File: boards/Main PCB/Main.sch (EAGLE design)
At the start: 89 parts, among them CN1 MINIB, CN2 MINIB, IC1 FT232RL, IC2 FT232RL, J1 3_PIN_JST-XH, J2 2_PIN_JST-XH, Q4 BSS138, Q5 BSS138, Q6 BSS138, Q7 BSS138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

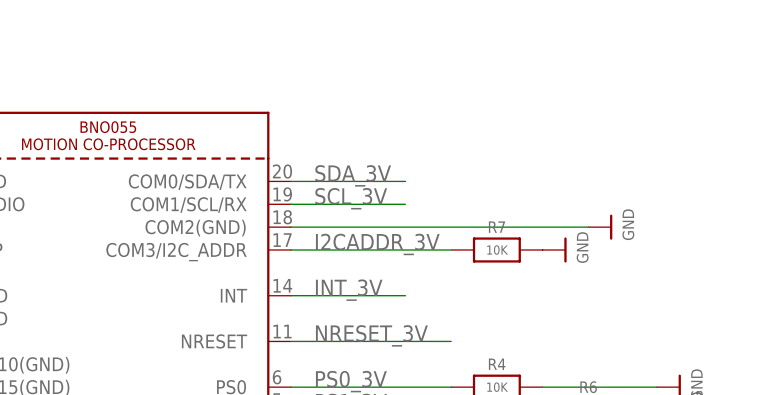
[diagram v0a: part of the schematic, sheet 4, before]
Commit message: Added pullup resistors for SDA and SCL
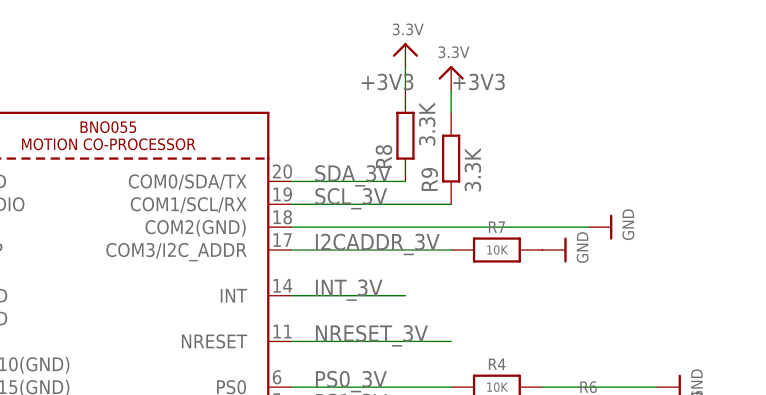
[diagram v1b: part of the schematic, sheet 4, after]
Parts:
- added R8, R9: 3.3K, resistor:R-EU_R0805
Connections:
- net +3V3: now also R8.2, R9.2
- net SCL_3V: now also R9.1
- net SDA_3V: now also R8.1
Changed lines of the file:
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@@
 <?xml version="1.0" encoding="utf-8"?>
 <!DOCTYPE eagle SYSTEM "eagle.dtd">
-<eagle version="9.2.2">
+<eagle version="9.3.1">
 <drawing>
 <settings>
@@
 <part name="JP4" library="microbuilder" deviceset="HEADER-1X4" device="76MIL"/>
 <part name="JP5" library="main_library" deviceset="MICROBUILDER_HEADER-1X6" device="76MIL"/>
+<part name="R8" library="resistor" library_urn="urn:adsk.eagle:library:348" deviceset="R-EU_" device="R0805" package3d_urn="urn:adsk.eagle:package:26059/1" value="3.3K"/>
+<part name="R9" library="resistor" library_urn="urn:adsk.eagle:library:348" deviceset="R-EU_" device="R0805" package3d_urn="urn:adsk.eagle:package:26059/1" value="3.3K"/>
+<part name="U$2" library="microbuilder" deviceset="3.3V" device=""/>
+<part name="U$4" library="microbuilder" deviceset="3.3V" device=""/>
 </parts>
 <sheets>
@@
 <attribute name="VALUE" x="-29.21" y="-71.12" size="1.778" layer="96"/>
 </instance>
+<instance part="R8" gate="G$1" x="-17.78" y="10.16" smashed="yes" rot="R90">
+<attribute name="NAME" x="-19.2786" y="6.35" size="1.778" layer="95" rot="R90"/>
+<attribute name="VALUE" x="-14.478" y="8.89" size="1.778" layer="96" rot="R90"/>
+</instance>
+<instance part="R9" gate="G$1" x="-12.7" y="7.62" smashed="yes" rot="R90">
+<attribute name="NAME" x="-14.1986" y="3.81" size="1.778" layer="95" rot="R90"/>
+<attribute name="VALUE" x="-9.398" y="3.81" size="1.778" layer="96" rot="R90"/>
+</instance>
+<instance part="U$2" gate="G$1" x="-17.78" y="20.32" smashed="yes">
+<attribute name="VALUE" x="-19.304" y="21.336" size="1.27" layer="96"/>
+</instance>
+<instance part="U$4" gate="G$1" x="-12.7" y="17.78" smashed="yes">
+<attribute name="VALUE" x="-14.224" y="18.796" size="1.27" layer="96"/>
+</instance>
 </instances>
 <busses>
@@
 <wire x1="-30.48" y1="5.08" x2="-17.78" y2="5.08" width="0.1524" layer="91"/>
 <label x="-27.94" y="5.08" size="1.778" layer="95"/>
+<pinref part="R8" gate="G$1" pin="1"/>
 </segment>
 <segment>
@@
 <segment>
 <pinref part="U$3" gate="G$1" pin="COM1/SCL/RX"/>
-<wire x1="-30.48" y1="2.54" x2="-17.78" y2="2.54" width="0.1524" layer="91"/>
+<wire x1="-30.48" y1="2.54" x2="-12.7" y2="2.54" width="0.1524" layer="91"/>
 <label x="-27.94" y="2.54" size="1.778" layer="95"/>
+<pinref part="R9" gate="G$1" pin="1"/>
 </segment>
 <segment>
@@
 <label x="-45.72" y="-55.88" size="1.778" layer="95"/>
 </segment>
-</net>
+<segment>
+<pinref part="R8" gate="G$1" pin="2"/>
+<pinref part="U$2" gate="G$1" pin="3.3V"/>
+<wire x1="-17.78" y1="17.78" x2="-17.78" y2="15.24" width="0.1524" layer="91"/>
+<label x="-22.86" y="15.24" size="1.778" layer="95"/>
+</segment>
+<segment>
+<pinref part="R9" gate="G$1" pin="2"/>
+<pinref part="U$4" gate="G$1" pin="3.3V"/>
+<wire x1="-12.7" y1="15.24" x2="-12.7" y2="12.7" width="0.1524" layer="91"/>
+<label x="-12.7" y="15.24" size="1.778" layer="95"/>
+</segment>
+</net>

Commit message: Added indicator LEDs to board and cleaned up iOS assets
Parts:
- added R10, R11, R32: 1K, rcl:R-US_R0805
- added RX2, RX3, RX4: Green, adafruit:LEDCHIP-LED0805
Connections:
- removed net TEST_GPIO4: U2.PB4/SPI1_MISO/TIM17_BKIN/TIM3_CH1/EVENTOUT
- new net N$12: R32.2, RX4.C
- new net N$13: RX2.C, U2.PB4/SPI1_MISO/TIM17_BKIN/TIM3_CH1/EVENTOUT
- new net N$3: R10.1, RX2.A
- new net N$4: R11.2, RX3.C
- net +3V3: now also R10.2, RX3.A
- net +5V: now also RX4.A
- net GND: now also R11.1, R32.1
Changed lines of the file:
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@@
 <?xml version="1.0" encoding="utf-8"?>
 <!DOCTYPE eagle SYSTEM "eagle.dtd">
-<eagle version="9.3.1">
+<eagle version="9.3.0">
 <drawing>
 <settings>
@@
 <part name="U$2" library="microbuilder" deviceset="3.3V" device=""/>
 <part name="U$4" library="microbuilder" deviceset="3.3V" device=""/>
+<part name="R10" library="rcl" library_urn="urn:adsk.eagle:library:334" deviceset="R-US_" device="R0805" package3d_urn="urn:adsk.eagle:package:23553/2" value="1K"/>
+<part name="RX2" library="adafruit" deviceset="LED" device="CHIP-LED0805" value="Green"/>
+<part name="+3V10" library="supply1" library_urn="urn:adsk.eagle:library:371" deviceset="+3V3" device=""/>
+<part name="RX3" library="adafruit" deviceset="LED" device="CHIP-LED0805" value="Green"/>
+<part name="R11" library="rcl" library_urn="urn:adsk.eagle:library:334" deviceset="R-US_" device="R0805" package3d_urn="urn:adsk.eagle:package:23553/2" value="1K"/>
+<part name="+3V11" library="supply1" library_urn="urn:adsk.eagle:library:371" deviceset="+3V3" device=""/>
+<part name="RX4" library="adafruit" deviceset="LED" device="CHIP-LED0805" value="Green"/>
+<part name="R32" library="rcl" library_urn="urn:adsk.eagle:library:334" deviceset="R-US_" device="R0805" package3d_urn="urn:adsk.eagle:package:23553/2" value="1K"/>
+<part name="GND33" library="supply1" library_urn="urn:adsk.eagle:library:371" deviceset="GND" device=""/>
 </parts>
 <sheets>
@@
 <attribute name="NAME" x="149.225" y="176.53" size="1.778" layer="95" rot="R90"/>
 <attribute name="VALUE" x="157.48" y="176.53" size="1.778" layer="96" rot="R90"/>
+</instance>
+<instance part="R10" gate="G$1" x="370.84" y="137.16" smashed="yes">
+<attribute name="VALUE" x="367.03" y="138.938" size="1.778" layer="96"/>
+</instance>
+<instance part="RX2" gate="G$1" x="360.68" y="137.16" smashed="yes" rot="R270">
+<attribute name="NAME" x="358.648" y="138.684" size="1.778" layer="95"/>
+<attribute name="VALUE" x="354.33" y="135.255" size="1.778" layer="96"/>
+</instance>
+<instance part="+3V10" gate="G$1" x="381" y="142.24" smashed="yes">
+<attribute name="VALUE" x="378.46" y="137.16" size="1.778" layer="96" rot="R90"/>
+</instance>
+<instance part="RX3" gate="G$1" x="370.84" y="198.12" smashed="yes">
+<attribute name="NAME" x="369.316" y="196.088" size="1.778" layer="95" rot="R90"/>
+<attribute name="VALUE" x="372.745" y="191.77" size="1.778" layer="96" rot="R90"/>
+</instance>
+<instance part="R11" gate="G$1" x="370.84" y="185.42" smashed="yes" rot="R90">
+<attribute name="VALUE" x="369.062" y="181.61" size="1.778" layer="96" rot="R90"/>
+</instance>
+<instance part="+3V11" gate="G$1" x="370.84" y="208.28" smashed="yes">
+<attribute name="VALUE" x="368.3" y="203.2" size="1.778" layer="96" rot="R90"/>
+</instance>
+<instance part="RX4" gate="G$1" x="22.86" y="254" smashed="yes">
+<attribute name="NAME" x="21.336" y="251.968" size="1.778" layer="95" rot="R90"/>
+<attribute name="VALUE" x="24.765" y="247.65" size="1.778" layer="96" rot="R90"/>
+</instance>
+<instance part="R32" gate="G$1" x="22.86" y="241.3" smashed="yes" rot="R90">
+<attribute name="VALUE" x="21.082" y="237.49" size="1.778" layer="96" rot="R90"/>
+</instance>
+<instance part="GND33" gate="1" x="22.86" y="231.14" smashed="yes">
+<attribute name="VALUE" x="20.32" y="228.6" size="1.778" layer="96"/>
 </instance>
 </instances>
@@
 <label x="406.4" y="101.6" size="1.778" layer="95" rot="R180"/>
 </segment>
+<segment>
+<pinref part="+3V10" gate="G$1" pin="+3V3"/>
+<wire x1="381" y1="137.16" x2="381" y2="139.7" width="0.1524" layer="91"/>
+<pinref part="R10" gate="G$1" pin="2"/>
+<wire x1="375.92" y1="137.16" x2="381" y2="137.16" width="0.1524" layer="91"/>
+</segment>
+<segment>
+<pinref part="RX3" gate="G$1" pin="A"/>
+<pinref part="+3V11" gate="G$1" pin="+3V3"/>
+<wire x1="370.84" y1="200.66" x2="370.84" y2="205.74" width="0.1524" layer="91"/>
+</segment>
 </net>
 <net name="N$34" class="0">
@@
 <pinref part="GND18" gate="1" pin="GND"/>
 <wire x1="365.76" y1="177.8" x2="368.3" y2="177.8" width="0.1524" layer="91"/>
+<pinref part="R11" gate="G$1" pin="1"/>
+<wire x1="370.84" y1="180.34" x2="370.84" y2="177.8" width="0.1524" layer="91"/>
+<wire x1="370.84" y1="177.8" x2="368.3" y2="177.8" width="0.1524" layer="91"/>
+<junction x="368.3" y="177.8"/>
 </segment>
 <segment>
@@
 <wire x1="419.1" y1="134.62" x2="414.02" y2="134.62" width="0.1524" layer="91"/>
 </segment>
+<segment>
+<pinref part="R32" gate="G$1" pin="1"/>
+<pinref part="GND33" gate="1" pin="GND"/>
+<wire x1="22.86" y1="236.22" x2="22.86" y2="233.68" width="0.1524" layer="91"/>
+</segment>
 </net>
 <net name="N$36" class="0">
@@
 <pinref part="IC3" gate="1" pin="OUT"/>
 <pinref part="P+1" gate="1" pin="+5V"/>
-<wire x1="20.32" y1="259.08" x2="25.4" y2="259.08" width="0.1524" layer="91"/>
+<wire x1="20.32" y1="259.08" x2="22.86" y2="259.08" width="0.1524" layer="91"/>
+<wire x1="22.86" y1="259.08" x2="25.4" y2="259.08" width="0.1524" layer="91"/>
 <wire x1="25.4" y1="259.08" x2="25.4" y2="266.7" width="0.1524" layer="91"/>
 <pinref part="C8" gate="G$1" pin="1"/>
@@
 <wire x1="27.94" y1="259.08" x2="35.56" y2="259.08" width="0.1524" layer="91"/>
 <junction x="27.94" y="259.08"/>
+<pinref part="RX4" gate="G$1" pin="A"/>
+<wire x1="22.86" y1="256.54" x2="22.86" y2="259.08" width="0.1524" layer="91"/>
+<junction x="22.86" y="259.08"/>
 </segment>
 <segment>
@@
 </segment>
 </net>
-<net name="TEST_GPIO4" class="0">
-<segment>
+<net name="N$4" class="0">
+<segment>
+<pinref part="RX3" gate="G$1" pin="C"/>
+<pinref part="R11" gate="G$1" pin="2"/>
+<wire x1="370.84" y1="193.04" x2="370.84" y2="190.5" width="0.1524" layer="91"/>
+</segment>
+</net>
+<net name="N$12" class="0">
+<segment>
+<pinref part="R32" gate="G$1" pin="2"/>
+<pinref part="RX4" gate="G$1" pin="C"/>
+<wire x1="22.86" y1="246.38" x2="22.86" y2="248.92" width="0.1524" layer="91"/>
+</segment>
+</net>
+<net name="N$3" class="0">
+<segment>
+<pinref part="R10" gate="G$1" pin="1"/>
+<pinref part="RX2" gate="G$1" pin="A"/>
+<wire x1="365.76" y1="137.16" x2="363.22" y2="137.16" width="0.1524" layer="91"/>
+</segment>
+</net>
+<net name="N$13" class="0">
+<segment>
+<pinref part="RX2" gate="G$1" pin="C"/>
 <pinref part="U2" gate="G$1" pin="PB4/SPI1_MISO/TIM17_BKIN/TIM3_CH1/EVENTOUT"/>
-<wire x1="350.52" y1="137.16" x2="358.14" y2="137.16" width="0.1524" layer="91"/>
-<label x="358.14" y="137.16" size="1.778" layer="95"/>
-</segment>
-</net>
+<wire x1="355.6" y1="137.16" x2="350.52" y2="137.16" width="0.1524" layer="91"/>
+</segment>
+</net>

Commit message: Cleaning up routing and labels for design review
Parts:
- R10, R11, R13, R14, R2, R3: value 1K -> 47
- R32: value 1K -> 100
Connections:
- net ENCODER1 renamed ADC_CH8
- net ENCODER2 renamed ADC_CH9
- net N$24 renamed SWDIO
- net N$28 renamed SWCLK
- net N$30 renamed SPI2_NSS_3V3
- net N$31 renamed SPI2_SCK_3V3
- net N$32 renamed SPI2_MISO_3V3
- net N$33 renamed SPI2_MOSI_3V3
- net N$35 renamed TX_JETSON
- net N$39 renamed RX_JETSON
- net N$47 renamed MOSI_5V
- net N$51 renamed MISO_5V
- net N$52 renamed SCK_5V
- net N$53 renamed NSS_5V
- removed net N$59: JP5.1
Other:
- note added: "10K"
- note added: "3.3V-5V Logic Converter For Display"
- note added: "Decoupling Capacitors"
- note added: "Encoder Connectors"
- note added: "External Oscillator"
- note added: "GPS UART Converter"
- note added: "IMU"
- note added: "Lidar UART Converter"
- note added: "Motor Controller UART Optical Isolator"
- note added: "Reset Circuitry"
- note added: "Ultrasonic 1"
- note added: "Ultrasonic 2"
- note added: "Ultrasonic 3"
- note removed: "GPS UART"

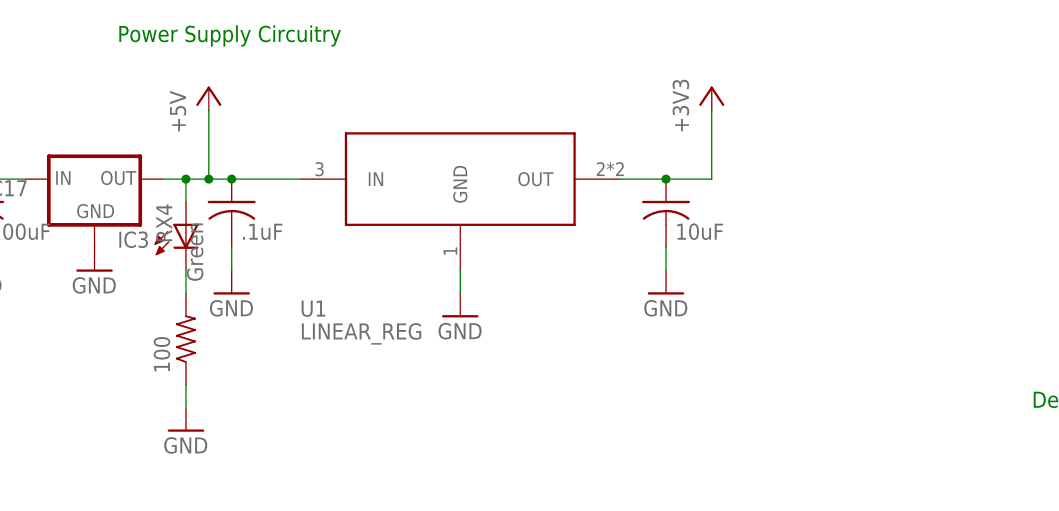
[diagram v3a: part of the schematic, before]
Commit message: Added a resettable fuse to the boards
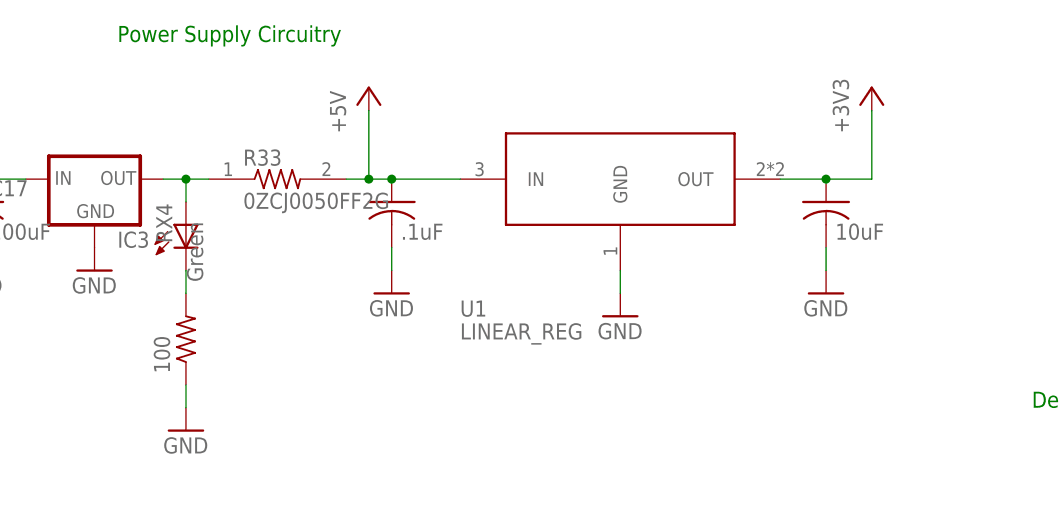
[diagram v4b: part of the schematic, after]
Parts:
- added R33: 0ZCJ0050FF2G, RESET_FUSE:0ZCJ0050FF2G
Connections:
- new net N$21: IC3.OUT, R33.1, RX4.A
- net +5V: now also R33.2; no longer IC3.OUT, RX4.A
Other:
- moved on the sheet: U1
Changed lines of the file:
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@@
 <part name="GND33" library="supply1" library_urn="urn:adsk.eagle:library:371" deviceset="GND" device=""/>
 <part name="U$6" library="microbuilder" deviceset="GND" device=""/>
+<part name="R33" library="RESET_FUSE" deviceset="0ZCJ0050FF2G" device=""/>
 </parts>
 <sheets>
@@
 <attribute name="VALUE" x="276.86" y="373.38" size="1.778" layer="96"/>
 </instance>
-<instance part="P+1" gate="1" x="312.42" y="393.7" smashed="yes">
-<attribute name="VALUE" x="309.88" y="388.62" size="1.778" layer="96" rot="R90"/>
-</instance>
-<instance part="U1" gate="G$1" x="340.36" y="383.54" smashed="yes">
-<attribute name="NAME" x="322.5434" y="368.2686" size="1.781659375" layer="95"/>
-<attribute name="VALUE" x="322.5453" y="365.7253" size="1.78146875" layer="96"/>
-</instance>
-<instance part="C8" gate="G$1" x="314.96" y="381" smashed="yes">
-<attribute name="VALUE" x="315.976" y="376.809" size="1.778" layer="96"/>
-</instance>
-<instance part="C9" gate="G$1" x="363.22" y="381" smashed="yes">
-<attribute name="VALUE" x="364.236" y="376.809" size="1.778" layer="96"/>
-</instance>
-<instance part="GND24" gate="1" x="314.96" y="370.84" smashed="yes">
-<attribute name="VALUE" x="312.42" y="368.3" size="1.778" layer="96"/>
-</instance>
-<instance part="GND25" gate="1" x="363.22" y="370.84" smashed="yes">
-<attribute name="VALUE" x="360.68" y="368.3" size="1.778" layer="96"/>
-</instance>
-<instance part="GND26" gate="1" x="340.36" y="368.3" smashed="yes">
-<attribute name="VALUE" x="337.82" y="365.76" size="1.778" layer="96"/>
-</instance>
-<instance part="+3V3" gate="G$1" x="368.3" y="393.7" smashed="yes">
-<attribute name="VALUE" x="365.76" y="388.62" size="1.778" layer="96" rot="R90"/>
+<instance part="P+1" gate="1" x="330.2" y="393.7" smashed="yes">
+<attribute name="VALUE" x="327.66" y="388.62" size="1.778" layer="96" rot="R90"/>
+</instance>
+<instance part="U1" gate="G$1" x="358.14" y="383.54" smashed="yes">
+<attribute name="NAME" x="340.3234" y="368.2686" size="1.781659375" layer="95"/>
+<attribute name="VALUE" x="340.3253" y="365.7253" size="1.78146875" layer="96"/>
+</instance>
+<instance part="C8" gate="G$1" x="332.74" y="381" smashed="yes">
+<attribute name="VALUE" x="333.756" y="376.809" size="1.778" layer="96"/>
+</instance>
+<instance part="C9" gate="G$1" x="381" y="381" smashed="yes">
+<attribute name="VALUE" x="382.016" y="376.809" size="1.778" layer="96"/>
+</instance>
+<instance part="GND24" gate="1" x="332.74" y="370.84" smashed="yes">
+<attribute name="VALUE" x="330.2" y="368.3" size="1.778" layer="96"/>
+</instance>
+<instance part="GND25" gate="1" x="381" y="370.84" smashed="yes">
+<attribute name="VALUE" x="378.46" y="368.3" size="1.778" layer="96"/>
+</instance>
+<instance part="GND26" gate="1" x="358.14" y="368.3" smashed="yes">
+<attribute name="VALUE" x="355.6" y="365.76" size="1.778" layer="96"/>
+</instance>
+<instance part="+3V3" gate="G$1" x="386.08" y="393.7" smashed="yes">
+<attribute name="VALUE" x="383.54" y="388.62" size="1.778" layer="96" rot="R90"/>
 </instance>
 <instance part="C17" gate="G$1" x="287.02" y="381" smashed="yes">
@@
 <instance part="U$6" gate="G$1" x="132.08" y="111.76" smashed="yes">
 <attribute name="VALUE" x="130.556" y="109.22" size="1.27" layer="96"/>
+</instance>
+<instance part="R33" gate="G$1" x="320.04" y="383.54" smashed="yes">
+<attribute name="NAME" x="316.23" y="385.0386" size="1.778" layer="95"/>
+<attribute name="VALUE" x="316.23" y="380.238" size="1.778" layer="96"/>
 </instance>
 </instances>
@@
 <pinref part="U1" gate="G$1" pin="OUT"/>
 <pinref part="C9" gate="G$1" pin="1"/>
-<wire x1="358.14" y1="383.54" x2="363.22" y2="383.54" width="0.1524" layer="91"/>
-<wire x1="363.22" y1="383.54" x2="368.3" y2="383.54" width="0.1524" layer="91"/>
-<junction x="363.22" y="383.54"/>
+<wire x1="375.92" y1="383.54" x2="381" y2="383.54" width="0.1524" layer="91"/>
+<wire x1="381" y1="383.54" x2="386.08" y2="383.54" width="0.1524" layer="91"/>
+<junction x="381" y="383.54"/>
 <pinref part="+3V3" gate="G$1" pin="+3V3"/>
-<wire x1="368.3" y1="383.54" x2="368.3" y2="391.16" width="0.1524" layer="91"/>
+<wire x1="386.08" y1="383.54" x2="386.08" y2="391.16" width="0.1524" layer="91"/>
 </segment>
 <segment>
@@
 <pinref part="C8" gate="G$1" pin="2"/>
 <pinref part="GND24" gate="1" pin="GND"/>
-<wire x1="314.96" y1="375.92" x2="314.96" y2="373.38" width="0.1524" layer="91"/>
+<wire x1="332.74" y1="375.92" x2="332.74" y2="373.38" width="0.1524" layer="91"/>
 </segment>
 <segment>
 <pinref part="C9" gate="G$1" pin="2"/>
 <pinref part="GND25" gate="1" pin="GND"/>
-<wire x1="363.22" y1="375.92" x2="363.22" y2="373.38" width="0.1524" layer="91"/>
+<wire x1="381" y1="375.92" x2="381" y2="373.38" width="0.1524" layer="91"/>
 </segment>
 <segment>
 <pinref part="U1" gate="G$1" pin="GND"/>
 <pinref part="GND26" gate="1" pin="GND"/>
-<wire x1="340.36" y1="373.38" x2="340.36" y2="370.84" width="0.1524" layer="91"/>
+<wire x1="358.14" y1="373.38" x2="358.14" y2="370.84" width="0.1524" layer="91"/>
 </segment>
 <segment>
@@
 <net name="+5V" class="0">
 <segment>
-<pinref part="IC3" gate="1" pin="OUT"/>
-<pinref part="P+1" gate="1" pin="+5V"/>
-<wire x1="307.34" y1="383.54" x2="309.88" y2="383.54" width="0.1524" layer="91"/>
-<wire x1="309.88" y1="383.54" x2="312.42" y2="383.54" width="0.1524" layer="91"/>
-<wire x1="312.42" y1="383.54" x2="312.42" y2="391.16" width="0.1524" layer="91"/>
-<pinref part="C8" gate="G$1" pin="1"/>
-<wire x1="312.42" y1="383.54" x2="314.96" y2="383.54" width="0.1524" layer="91"/>
-<junction x="312.42" y="383.54"/>
-<pinref part="U1" gate="G$1" pin="IN"/>
-<wire x1="314.96" y1="383.54" x2="322.58" y2="383.54" width="0.1524" layer="91"/>
-<junction x="314.96" y="383.54"/>
-<pinref part="RX4" gate="G$1" pin="A"/>
-<wire x1="309.88" y1="381" x2="309.88" y2="383.54" width="0.1524" layer="91"/>
-<junction x="309.88" y="383.54"/>
-</segment>
-<segment>
 <pinref part="R19" gate="G$1" pin="2"/>
 <pinref part="P+2" gate="1" pin="+5V"/>
@@
 <junction x="477.52" y="248.92"/>
 <label x="474.98" y="248.92" size="1.778" layer="95" rot="R180"/>
+</segment>
+<segment>
+<pinref part="R33" gate="G$1" pin="2"/>
+<pinref part="C8" gate="G$1" pin="1"/>
+<wire x1="327.66" y1="383.54" x2="330.2" y2="383.54" width="0.1524" layer="91"/>
+<pinref part="U1" gate="G$1" pin="IN"/>
+<wire x1="330.2" y1="383.54" x2="332.74" y2="383.54" width="0.1524" layer="91"/>
+<wire x1="332.74" y1="383.54" x2="340.36" y2="383.54" width="0.1524" layer="91"/>
+<junction x="332.74" y="383.54"/>
+<pinref part="P+1" gate="1" pin="+5V"/>
+<wire x1="330.2" y1="391.16" x2="330.2" y2="383.54" width="0.1524" layer="91"/>
+<junction x="330.2" y="383.54"/>
 </segment>
 </net>
@@
 </segment>
 </net>
+<net name="N$21" class="0">
+<segment>
+<pinref part="IC3" gate="1" pin="OUT"/>
+<wire x1="307.34" y1="383.54" x2="309.88" y2="383.54" width="0.1524" layer="91"/>
+<wire x1="309.88" y1="383.54" x2="312.42" y2="383.54" width="0.1524" layer="91"/>
+<pinref part="RX4" gate="G$1" pin="A"/>
+<wire x1="309.88" y1="381" x2="309.88" y2="383.54" width="0.1524" layer="91"/>
+<junction x="309.88" y="383.54"/>
+<pinref part="R33" gate="G$1" pin="1"/>
+</segment>
+</net>
